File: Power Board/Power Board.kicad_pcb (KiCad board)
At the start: 4 copper layers, 197 parts, among them IC1 LTC4151IMS#PBF, IC2 LTC4151IMS#PBF, J1 Conn_01x02, J10 Conn_01x02, J11 Conn_01x02, J12 Conn_01x02, J13 Conn_01x02, J14 Conn_01x02, J15 Conn_01x02, J16 Conn_01x02, J17 Conn_01x02, J18 Conn_02x03_Top_Bottom, J2 Conn_01x02, J20 Conn_02x03_Top_Bottom, J3 Conn_01x02, J4 Conn_01x02, J5 Conn_01x02, J6 Conn_01x02, J7 Conn_01x02, J8 Conn_01x02, J9 Conn_02x03_Top_Bottom, Q1 Q_PMOS_GDS, Q10 Q_NMOS_GDS, Q11 Q_NMOS_GDS, Q12 Q_NMOS_GDS, Q13 Q_NMOS_GDS, Q14 Q_NMOS_GDS, Q15 Q_NMOS_GDS, Q16 Q_NMOS_GDS, Q17 Q_NMOS_GDS, Q18 Q_NMOS_GDS, Q19 Q_NMOS_GDS, Q2 Q_PMOS_GDS, Q20 Q_NMOS_GDS, Q21 Q_NMOS_GDS, Q22 Q_NMOS_GDS, Q3 Q_PMOS_GDS, Q4 Q_PMOS_GDS, Q5 Q_PMOS_GDS, Q6 Q_PMOS_GDS, Q7 Q_PMOS_GDS, Q8 Q_PMOS_GDS, Q9 Q_NMOS_GDS, U1 LTC4372CDD-PBF, U10 ACS770xCB-050U-PFF, U11 ACS770xCB-050U-PFF, U12 ACS770xCB-050U-PFF, U13 ACS770xCB-050U-PFF, U14 ACS770xCB-050U-PFF, U15 ADC128S052CIMT, U16 ADC128S052CIMT, U17 TLV70033_SOT23-5, U2 LTC4372CDD-PBF, U3 LTC4372CDD-PBF, U4 LTC4372CDD-PBF, U5 LTC4372CDD-PBF, U6 LTC4372CDD-PBF, U7 LTC4372CDD-PBF, U8 ACS770xCB-050U-PFF, U9 ACS770xCB-050U-PFF

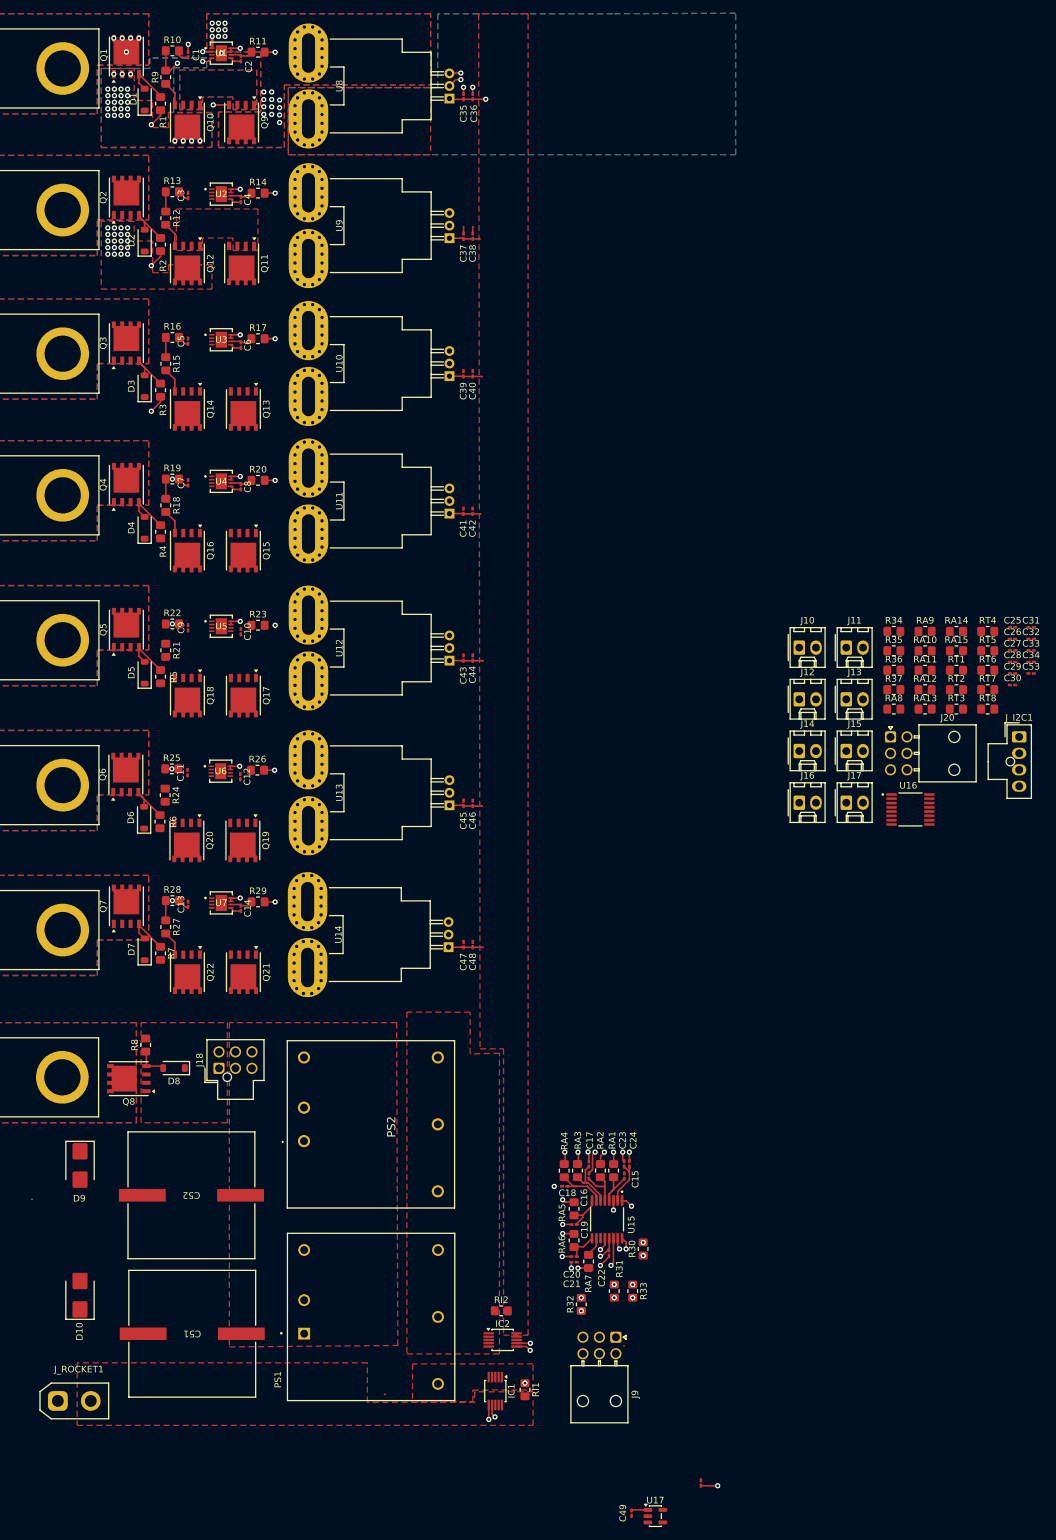
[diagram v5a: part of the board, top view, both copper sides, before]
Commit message: i2c routing
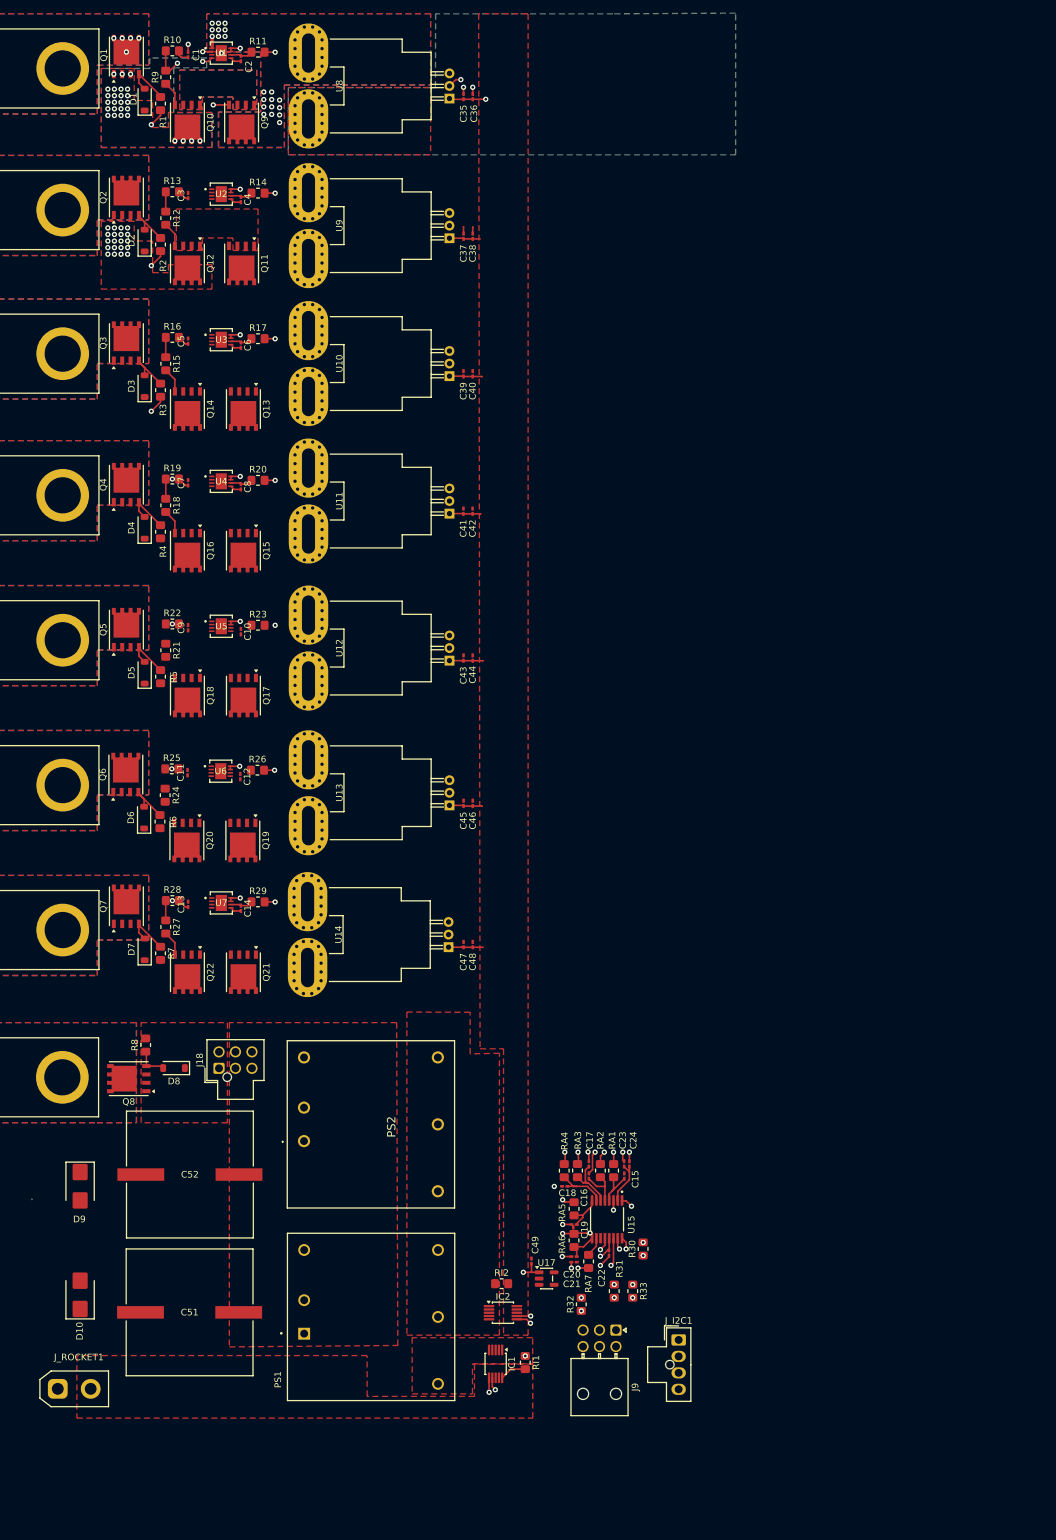
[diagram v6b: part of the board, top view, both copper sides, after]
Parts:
- removed C25, C26, C27, C28, C29, C30, C31, C53: 22 nF, Capacitor_SMD:C_0201_0603Metric_Pad0.64x0.40mm_HandSolder
- removed C32, C33: 0.1 uF, Capacitor_SMD:C_0201_0603Metric_Pad0.64x0.40mm_HandSolder
- removed C34: 1 uF, Capacitor_SMD:C_0201_0603Metric_Pad0.64x0.40mm_HandSolder
- removed J10, J11, J12, J13, J14, J15, J16, J17: Conn_01x02, Connector_Molex:Molex_KK-254_AE-6410-02A_1x02_P2.54mm_Vertical
- removed J20: Conn_02x03_Top_Bottom, Connector_Molex:Molex_Nano-Fit_105314-xx06_2x03_P2.50mm_Horizontal
- removed R34, R35, R36, R37: 33, Resistor_SMD:R_0805_2012Metric_Pad1.20x1.40mm_HandSolder
- removed RA10, RA11, RA12, RA13, RA14, RA15, RA8, RA9: 100, Resistor_SMD:R_0805_2012Metric_Pad1.20x1.40mm_HandSolder
- removed RT1, RT2, RT3, RT4, RT5, RT6, RT7, RT8: 2.7K, Resistor_SMD:R_0805_2012Metric_Pad1.20x1.40mm_HandSolder
- removed U16: ADC128S052CIMT, ADC128S052CIMT_NOPB:SOP65P640X120-16N
- moved J_I2C1 105.1 mm to (190.3, 229.5)
- moved C50 43.0 mm to (174.3, 212.9)
- moved C49 41.1 mm to (167.9, 217.6), turned to 90 degrees
- moved U17 39.7 mm to (170.2, 220.2)
- moved IC1 4.13 mm to (162.5, 233.2)
- moved RI2 4.13 mm to (163.4, 221.0)
- moved IC2 4.13 mm to (163.6, 225.4)
- moved RI1 4.13 mm to (167.0, 233.0)
- moved C51 3.28 mm to (116.0, 225.3)
- moved C52 3.16 mm to (116.1, 204.4)
- moved D9 3.15 mm to (99.4, 206.2)
- moved J_ROCKET1 1.84 mm to (96.0, 237.0)
- moved J9 1.09 mm to (180.7, 228.0)
- moved D10 0.07 mm to (99.4, 222.7)
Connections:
- J_I2C1 pad 2: /SCL -> GNDD
- J_I2C1 pad 4: GNDD -> /SCL
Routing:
- net /SCL: track 4.52 -> 47.8 mm
- net /SDA: track 4.11 -> 43.3 mm
- net /24V_REGULATED: track 0.00 -> 4.04 mm
- net /BATT_1_SENSE: track 177.6 -> 175.8 mm, vias 2 -> 1
- net Net-(J9-Pin_6): track 10.8 -> 9.39 mm
- net /5V_REGULATED: track 46.1 -> 47.3 mm, vias 1 -> 2
- net Net-(J9-Pin_4): track 16.7 -> 15.5 mm
- net Net-(J9-Pin_1): track 7.10 -> 5.96 mm
- net Net-(J9-Pin_3): track 4.10 -> 3.02 mm

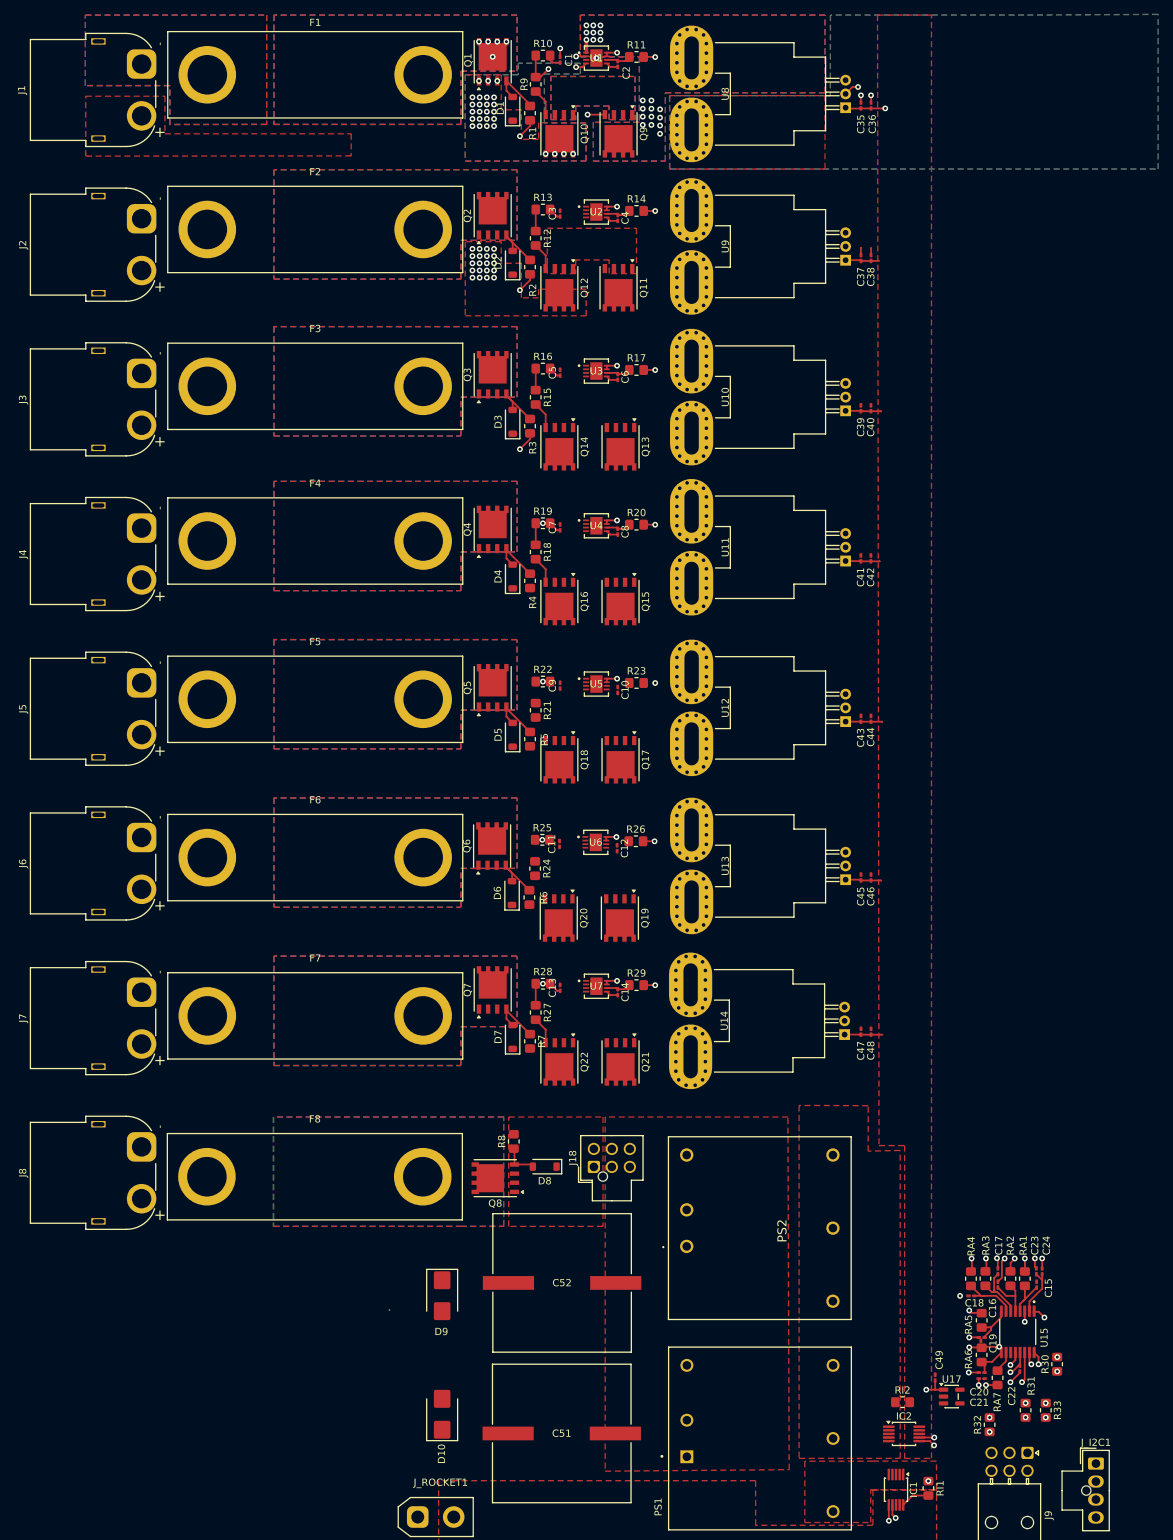
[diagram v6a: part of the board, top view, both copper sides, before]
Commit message: added M3 mounting holes, removed buck converter (to be replaced with half-brick), added more pours
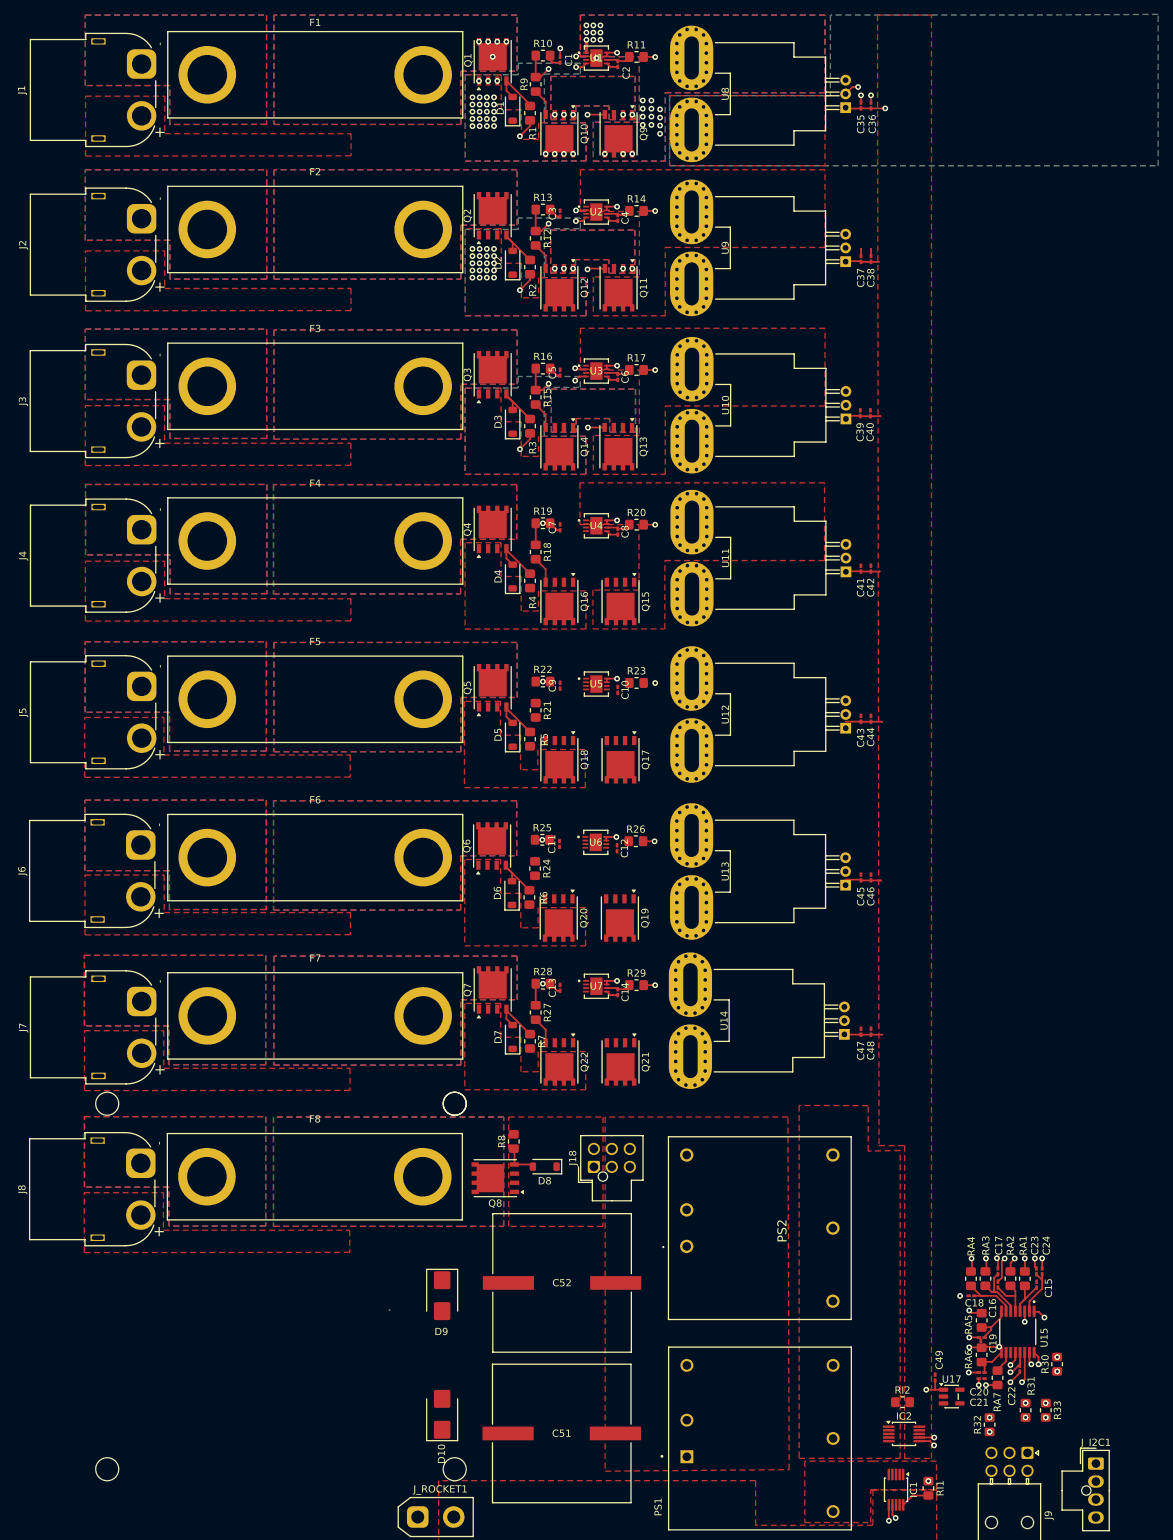
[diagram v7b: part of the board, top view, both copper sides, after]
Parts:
- added ? (x2): , , F.Cu at (101.1, 179.5)
- added ?: , , F.Cu at (101.1, 230.3)
- added ?: , , F.Cu at (52.8, 179.5)
- added ?: , , F.Cu at (52.8, 230.3)
- moved J8 2.28 mm to (57.5, 187.8)
- moved U11 1.50 mm to (155.5, 105.6)
- moved C41 1.42 mm to (157.6, 105.1)
- moved C42 1.42 mm to (159.0, 105.1)
- moved J7 1.29 mm to (57.6, 165.3)
- moved U10 1.12 mm to (155.5, 84.3)
- moved J6 1.05 mm to (57.5, 143.6)
- moved U12 0.92 mm to (155.5, 127.3)
- moved U13 0.76 mm to (155.5, 149.1)
- moved C39 0.70 mm to (157.5, 83.5)
- moved C40 0.70 mm to (158.9, 83.5)
- moved J5 0.49 mm to (57.6, 121.5)
- moved Q13 0.30 mm to (123.9, 88.2)
- moved J3 0.24 mm to (57.6, 78.2)
- moved J4 0.22 mm to (57.6, 99.7)
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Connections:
- F7 pad 1: Net-(J7-Pin_2) -> Net-(J7-Pin_1)
- J7 pad 1: GND -> Net-(J7-Pin_1)
- J7 pad 2: Net-(J7-Pin_2) -> GND
- PS2 pad 1: /24V_UNREGULATED -> unconnected-(PS2-+VIN-Pad1)
- PS2 pad 2: GND -> unconnected-(PS2--VIN-Pad2)
- PS2 pad 4: GND -> unconnected-(PS2-+VOUT-Pad4)
- PS2 pad 6: /5V_PSO -> unconnected-(PS2--VOUT-Pad6)
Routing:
- net Net-(Q11-G): track 3.00 -> 22.2 mm, vias 0 -> 3
- net Net-(Q13-G): track 3.00 -> 22.0 mm, vias 0 -> 3
- net /SHDN: track 165.6 -> 167.4 mm
- net /BATT_IN_12_3: track 0.00 -> 1.74 mm, vias 0 -> 1
- net /BATT_IN_12_2: track 0.00 -> 1.61 mm, vias 20 -> 21
- net /BATT_3_SENSE: track 132.9 -> 131.7 mm
- net /BATT_5_SENSE: track 94.6 -> 93.7 mm
- net /BATT_6_SENSE: track 78.6 -> 77.9 mm
- net /BATT_4_SENSE: track 109.9 -> 109.1 mm
- net Net-(Q11-S): vias 0 -> 5
- net Net-(Q10-S): vias 0 -> 5
- net /BATT_1_PRESENSE: vias 21 -> 24
- added copper zone on F.Cu, net /BATT_2_PRESENSE
- added copper zone on F.Cu, net /BATT_3_PRESENSE
- added copper zone on F.Cu, net /BATT_4_PRESENSE
- added copper zone on B.Cu, net /BATT_IN_12_2
- added copper zone on B.Cu, net /BATT_IN_12_3
- added copper zone on F.Cu, net /BATT_IN_12_3
- added copper zone on F.Cu, net /BATT_IN_12_4
- added copper zone on F.Cu, net /BATT_IN_12_5
- added copper zone on F.Cu, net /BATT_IN_12_6
- added copper zone on F.Cu, net /BATT_IN_12_7
- added copper zone on B.Cu, net Net-(J1-Pin_1)
- added copper zone on F.Cu, net Net-(J1-Pin_1)
- added copper zone on B.Cu, net Net-(J2-Pin_1)
- added copper zone on F.Cu, net Net-(J2-Pin_1)
- added copper zone on B.Cu, net Net-(J3-Pin_1)
- added copper zone on F.Cu, net Net-(J3-Pin_1)
- added copper zone on B.Cu, net Net-(J4-Pin_1)
- added copper zone on F.Cu, net Net-(J4-Pin_1)
- added copper zone on B.Cu, net Net-(J5-Pin_1)
- added copper zone on F.Cu, net Net-(J5-Pin_1)
- added copper zone on B.Cu, net Net-(J6-Pin_1)
- added copper zone on F.Cu, net Net-(J6-Pin_1)
- added copper zone on B.Cu, net Net-(J7-Pin_1)
- added copper zone on F.Cu, net Net-(J7-Pin_1)
- added copper zone on B.Cu, net Net-(J8-Pin_1)
- added copper zone on F.Cu, net Net-(J8-Pin_1)
- added copper zone on B.Cu, net Net-(Q11-S)
- added copper zone on B.Cu, net Net-(Q13-S)
- added copper zone on F.Cu, net Net-(Q13-S)
- removed copper zone on B.Cu, net GND
